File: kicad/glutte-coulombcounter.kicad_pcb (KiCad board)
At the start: 2 copper layers, 100 x 85 mm, 72 parts, among them J1 12V, J2 Measure, J3 K1, J4 AVR-ISP-6, J5 Glutte, J6 K2, J7 K3, J8 Raspi, K1 G6SK-2F-DC5, K2 G6SK-2F-DC5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

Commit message: Minor routing changes
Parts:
- moved C19 2.05 mm to (81.8, 84.1), turned to 270 degrees
- moved C14 0.81 mm to (81.8, 91.4)
- moved C17 0.63 mm to (81.8, 87.6)
- moved C18 0.59 mm to (84.1, 92.5)
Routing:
- net Net-(C19-Pad2): track 5.55 -> 3.92 mm
- net Net-(C18-Pad1): track 7.34 -> 6.15 mm
- net Net-(C14-Pad2): track 4.57 -> 3.97 mm
- net Net-(C14-Pad1): track 4.29 -> 3.69 mm
- net Net-(C17-Pad2): track 4.26 -> 3.75 mm
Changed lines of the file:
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@@
     (thickness 1.6)
     (drawings 152)
-    (tracks 813)
+    (tracks 811)
     (zones 0)
     (modules 72)
@@
   )
   (setup
-    (last_trace_width 0.2)
+    (last_trace_width 0.25)
     (user_trace_width 0.2)
     (user_trace_width 0.25)
@@
     (add_net "Net-(FB1-Pad2)")
     (add_net "Net-(FB2-Pad2)")
-    (add_net "Net-(J5-Pad1)")
     (add_net "Net-(J5-Pad2)")
     (add_net "Net-(J5-Pad3)")
-    (add_net "Net-(J5-Pad4)")
-    (add_net "Net-(J5-Pad6)")
-    (add_net "Net-(J5-Pad7)")
-    (add_net "Net-(J5-Pad8)")
-    (add_net "Net-(J5-Pad9)")
-    (add_net "Net-(J8-Pad1)")
     (add_net "Net-(J8-Pad2)")
     (add_net "Net-(J8-Pad3)")
-    (add_net "Net-(J8-Pad4)")
-    (add_net "Net-(J8-Pad6)")
-    (add_net "Net-(J8-Pad7)")
-    (add_net "Net-(J8-Pad8)")
-    (add_net "Net-(J8-Pad9)")
     (add_net "Net-(K1-Pad12)")
     (add_net "Net-(K1-Pad7)")
@@
     (add_net "Net-(R5-Pad1)")
     (add_net "Net-(R7-Pad1)")
-    (add_net "Net-(U2-Pad1)")
-    (add_net "Net-(U2-Pad3)")
-    (add_net "Net-(U2-Pad5)")
-    (add_net "Net-(U2-Pad7)")
-    (add_net "Net-(U2-Pad8)")
-    (add_net "Net-(U4-Pad4)")
     (add_net "Net-(U6-Pad13)")
     (add_net "Net-(U6-Pad8)")
-    (add_net "Net-(U7-Pad13)")
-    (add_net "Net-(U7-Pad15)")
-    (add_net "Net-(U7-Pad4)")
-    (add_net "Net-(U7-Pad5)")
-    (add_net "Net-(U9-Pad10)")
     (add_net VREF)
   )
@@
   )
   (module Capacitor_SMD:C_0805_2012Metric (layer F.Cu)
-    (at 83.566 83.058 180)
+    (at 81.788 84.074 270)
     (descr "Capacitor SMD 0805 (2012 Metric), square (rectangular) end terminal, IPC_7351 nominal, (Body size source: https://docs.google.com/spreadsheets/d/1BsfQQcO9C6DZCsRaXUlFlo91Tg2WpOkGARC1WS5S8t0/edit?usp=sharing), generated with kicad-footprint-generator")
     (tags capacitor)
     (attr smd)
-    (fp_text reference C19 (at 0 -1.65) (layer F.SilkS)
+    (fp_text reference C19 (at 0 -1.65 90) (layer F.SilkS)
       (effects (font (size 1 1) (thickness 0.15)))
     )
-    (fp_text value 1u (at 0 1.65) (layer F.Fab)
+    (fp_text value 1u (at 0 1.65 90) (layer F.Fab)
       (effects (font (size 1 1) (thickness 0.15)))
     )
-    (fp_text user %R (at 0 0) (layer F.Fab)
+    (fp_text user %R (at 0 0 90) (layer F.Fab)
       (effects (font (size 0.5 0.5) (thickness 0.08)))
     )
@@
     (fp_line (start -1 -0.6) (end 1 -0.6) (layer F.Fab) (width 0.1))
     (fp_line (start -1 0.6) (end -1 -0.6) (layer F.Fab) (width 0.1))
-    (pad 2 smd roundrect (at 0.9375 0 180) (size 0.975 1.4) (layers F.Cu F.Paste F.Mask) (roundrect_rratio 0.25)
+    (pad 2 smd roundrect (at 0.9375 0 270) (size 0.975 1.4) (layers F.Cu F.Paste F.Mask) (roundrect_rratio 0.25)
       (net 18 "Net-(C19-Pad2)"))
-    (pad 1 smd roundrect (at -0.9375 0 180) (size 0.975 1.4) (layers F.Cu F.Paste F.Mask) (roundrect_rratio 0.25)
+    (pad 1 smd roundrect (at -0.9375 0 270) (size 0.975 1.4) (layers F.Cu F.Paste F.Mask) (roundrect_rratio 0.25)
       (net 1 GNDA))
     (model ${KISYS3DMOD}/Capacitor_SMD.3dshapes/C_0805_2012Metric.wrl
@@
   )
   (module Capacitor_SMD:C_0805_2012Metric (layer F.Cu)
-    (at 84.608 92.202 270)
+    (at 84.074 92.456 270)
     (descr "Capacitor SMD 0805 (2012 Metric), square (rectangular) end terminal, IPC_7351 nominal, (Body size source: https://docs.google.com/spreadsheets/d/1BsfQQcO9C6DZCsRaXUlFlo91Tg2WpOkGARC1WS5S8t0/edit?usp=sharing), generated with kicad-footprint-generator")
     (tags capacitor)
@@
   )
   (module Capacitor_SMD:C_0805_2012Metric (layer F.Cu)
-    (at 82.068 87.065 90)
+    (at 81.788 87.63 90)
     (descr "Capacitor SMD 0805 (2012 Metric), square (rectangular) end terminal, IPC_7351 nominal, (Body size source: https://docs.google.com/spreadsheets/d/1BsfQQcO9C6DZCsRaXUlFlo91Tg2WpOkGARC1WS5S8t0/edit?usp=sharing), generated with kicad-footprint-generator")
     (tags capacitor)
     (attr smd)
-    (fp_text reference C17 (at 0 -1.65 90) (layer F.SilkS)
+    (fp_text reference C17 (at 0 1.778 90) (layer F.SilkS)
       (effects (font (size 1 1) (thickness 0.15)))
     )
@@
   )
   (module Capacitor_SMD:C_0805_2012Metric (layer F.Cu)
-    (at 82.068 92.202 90)
+    (at 81.788 91.44 90)
     (descr "Capacitor SMD 0805 (2012 Metric), square (rectangular) end terminal, IPC_7351 nominal, (Body size source: https://docs.google.com/spreadsheets/d/1BsfQQcO9C6DZCsRaXUlFlo91Tg2WpOkGARC1WS5S8t0/edit?usp=sharing), generated with kicad-footprint-generator")
     (tags capacitor)
     (attr smd)
-    (fp_text reference C14 (at 0 -1.65 90) (layer F.SilkS)
+    (fp_text reference C14 (at -2.54 -0.254 180) (layer F.SilkS)
       (effects (font (size 1 1) (thickness 0.15)))
     )
@@
   (via (at 80.264 95.504) (size 0.8) (drill 0.4) (layers F.Cu B.Cu) (net 1))
   (via (at 71.882 93.98) (size 0.8) (drill 0.4) (layers F.Cu B.Cu) (net 1))
-  (via (at 86.106 92.71) (size 0.8) (drill 0.4) (layers F.Cu B.Cu) (net 1))
-  (via (at 87.884 83.058) (size 0.8) (drill 0.4) (layers F.Cu B.Cu) (net 1))
+  (via (at 84.074 94.742) (size 0.8) (drill 0.4) (layers F.Cu B.Cu) (net 1))
+  (via (at 81.788 81.534) (size 0.8) (drill 0.4) (layers F.Cu B.Cu) (net 1))
   (via (at 85.09 66.04) (size 0.8) (drill 0.4) (layers F.Cu B.Cu) (net 1))
   (via (at 97.5 95) (size 0.8) (drill 0.4) (layers F.Cu B.Cu) (net 1))
@@
   (segment (start 56.8175 61.468) (end 60.2345 61.468) (width 0.4) (layer F.Cu) (net 11))
   (segment (start 60.2345 61.468) (end 60.325 61.3775) (width 0.4) (layer F.Cu) (net 11))
-  (segment (start 80.3805 89.605) (end 82.068 91.2925) (width 0.25) (layer F.Cu) (net 12))
-  (segment (start 78.193 89.605) (end 80.3805 89.605) (width 0.25) (layer F.Cu) (net 12))
-  (segment (start 78.193 92.145) (end 79.9455 92.145) (width 0.25) (layer F.Cu) (net 13))
-  (segment (start 80.94 93.1395) (end 82.068 93.1395) (width 0.25) (layer F.Cu) (net 13))
-  (segment (start 79.9455 92.145) (end 80.94 93.1395) (width 0.25) (layer F.Cu) (net 13))
+  (segment (start 80.5965 90.5025) (end 81.788 90.5025) (width 0.25) (layer F.Cu) (net 12))
+  (segment (start 78.193 89.605) (end 79.699 89.605) (width 0.25) (layer F.Cu) (net 12))
+  (segment (start 79.699 89.605) (end 80.5965 90.5025) (width 0.25) (layer F.Cu) (net 12))
+  (segment (start 81.5555 92.145) (end 81.788 92.3775) (width 0.25) (layer F.Cu) (net 13))
+  (segment (start 78.193 92.145) (end 81.5555 92.145) (width 0.25) (layer F.Cu) (net 13))
   (via (at 44.196 59.436) (size 0.8) (drill 0.4) (layers F.Cu B.Cu) (net 14))
   (segment (start 44.45 59.69) (end 44.45 61.7) (width 0.25) (layer F.Cu) (net 14))
@@
   (segment (start 74.7545 43.18) (end 78.105 43.18) (width 0.4) (layer F.Cu) (net 14))
   (segment (start 74.676 43.2585) (end 74.7545 43.18) (width 0.4) (layer F.Cu) (net 14))
-  (segment (start 81.518 86.1275) (end 82.068 86.1275) (width 0.25) (layer F.Cu) (net 15))
-  (segment (start 78.193 87.065) (end 80.5805 87.065) (width 0.25) (layer F.Cu) (net 15))
-  (segment (start 80.5805 87.065) (end 81.518 86.1275) (width 0.25) (layer F.Cu) (net 15))
-  (segment (start 81.7355 88.335) (end 82.068 88.0025) (width 0.25) (layer F.Cu) (net 16))
-  (segment (start 78.193 88.335) (end 81.7355 88.335) (width 0.25) (layer F.Cu) (net 16))
-  (segment (start 83.836653 92.063847) (end 84.608 91.2925) (width 0.25) (layer F.Cu) (net 17))
-  (segment (start 81.07681 92.202) (end 83.6985 92.202) (width 0.25) (layer F.Cu) (net 17))
-  (segment (start 78.193 90.875) (end 79.74981 90.875) (width 0.25) (layer F.Cu) (net 17))
-  (segment (start 83.6985 92.202) (end 83.836653 92.063847) (width 0.25) (layer F.Cu) (net 17))
-  (segment (start 79.74981 90.875) (end 81.07681 92.202) (width 0.25) (layer F.Cu) (net 17))
-  (segment (start 79.870002 85.795) (end 82.607002 83.058) (width 0.25) (layer F.Cu) (net 18))
-  (segment (start 78.193 85.795) (end 79.870002 85.795) (width 0.25) (layer F.Cu) (net 18))
+  (segment (start 78.193 87.065) (end 80.067 87.065) (width 0.25) (layer F.Cu) (net 15))
+  (segment (start 80.4395 86.6925) (end 81.788 86.6925) (width 0.25) (layer F.Cu) (net 15))
+  (segment (start 80.067 87.065) (end 80.4395 86.6925) (width 0.25) (layer F.Cu) (net 15))
+  (segment (start 80.1855 88.5675) (end 81.788 88.5675) (width 0.25) (layer F.Cu) (net 16))
+  (segment (start 78.193 88.335) (end 79.953 88.335) (width 0.25) (layer F.Cu) (net 16))
+  (segment (start 79.953 88.335) (end 80.1855 88.5675) (width 0.25) (layer F.Cu) (net 16))
+  (segment (start 78.8365 91.5185) (end 84.074 91.5185) (width 0.25) (layer F.Cu) (net 17))
+  (segment (start 78.193 90.875) (end 78.8365 91.5185) (width 0.25) (layer F.Cu) (net 17))
+  (segment (start 81.0045 85.795) (end 81.788 85.0115) (width 0.25) (layer F.Cu) (net 18))
+  (segment (start 78.193 85.795) (end 81.0045 85.795) (width 0.25) (layer F.Cu) (net 18))
   (segment (start 63.246 29.126) (end 63.246 25.599) (width 0.4) (layer F.Cu) (net 19))
   (segment (start 61.957 29.49) (end 62.882 29.49) (width 0.4) (layer F.Cu) (net 19))

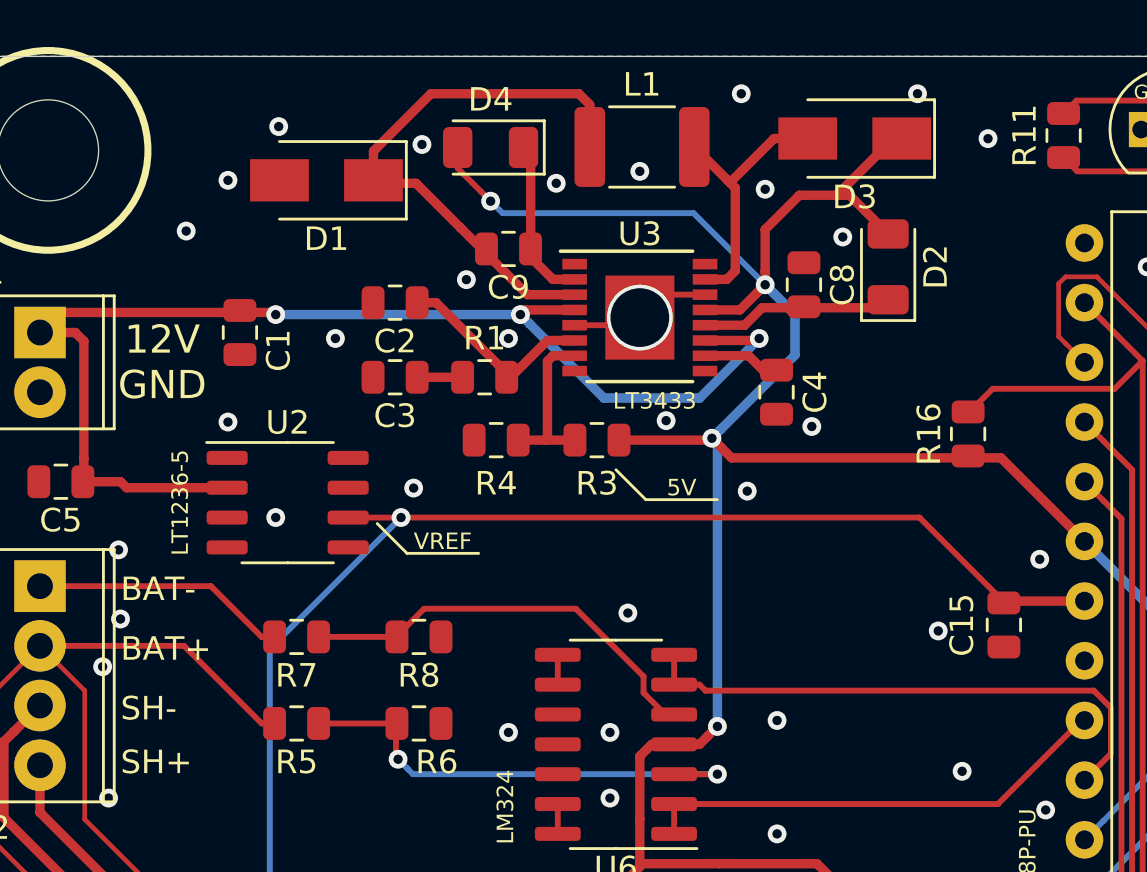
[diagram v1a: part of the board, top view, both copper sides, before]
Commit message: Correct wrong DCDC inductor
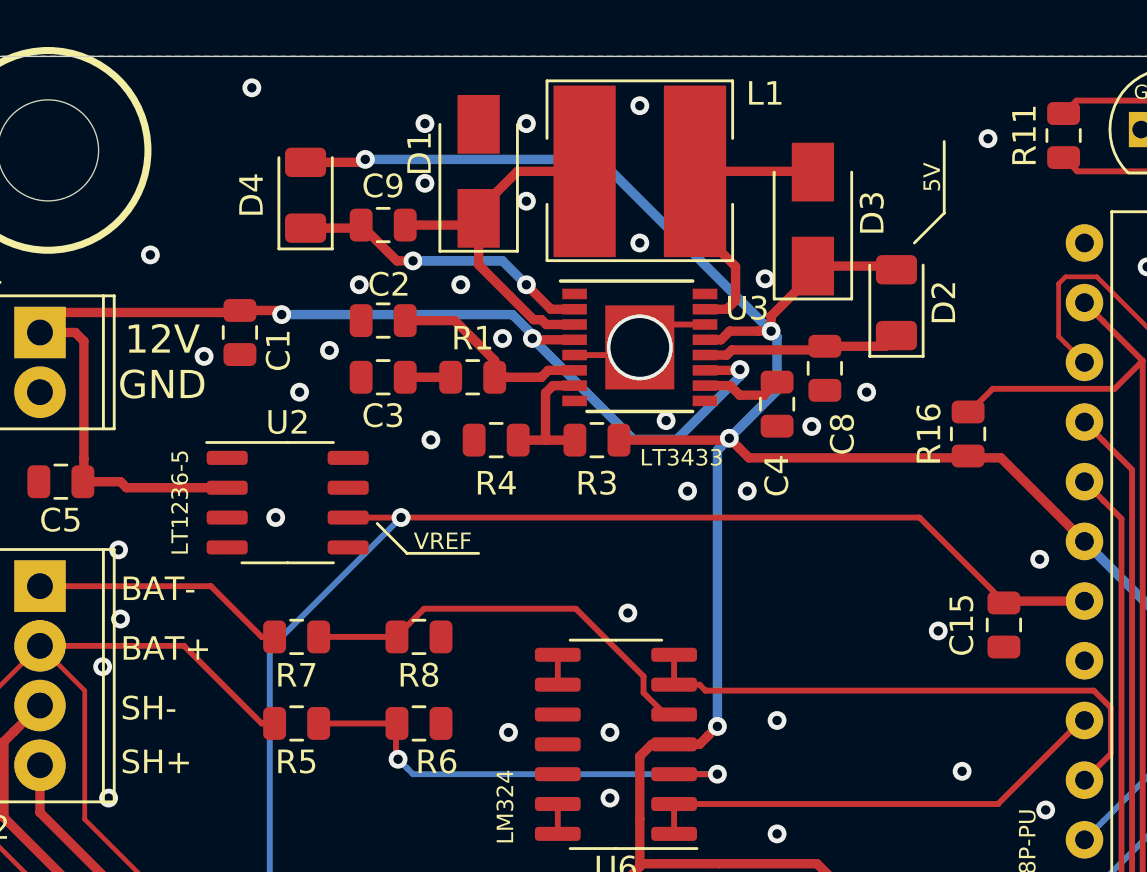
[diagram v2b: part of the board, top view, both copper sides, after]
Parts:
- L1: footprint Inductor_SMD:L_1812_4532Metric_Pad1.30x3.40mm_HandSolder -> glutte-coulombcounter:Sumida_CDRH6D28
- moved D4 8.13 mm to (45.0, 25.9), turned to 90 degrees
- moved D1 6.49 mm to (52.3, 24.9), turned to 90 degrees
- moved C9 5.43 mm to (48.3, 27.2), turned to 0 degrees
- moved D3 3.86 mm to (66.5, 26.9), turned to 90 degrees
- moved C8 3.67 mm to (67.1, 33.3), turned to 90 degrees
- moved D2 1.56 mm to (70.1, 30.5)
- moved U3 1.27 mm to (59.2, 32.4)
- moved L1 1.04 mm to (59.2, 24.9)
- moved C2 0.92 mm to (48.3, 31.2)
- moved C4 0.51 mm to (65.0, 34.8)
- moved C3 0.51 mm to (48.3, 33.7)
- moved R1 0.51 mm to (52.1, 33.7)
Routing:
- net Net-(C9-Pad2): track 24.0 -> 15.9 mm
- net Net-(C9-Pad1): track 7.06 -> 13.0 mm, vias 0 -> 2
- net +5VA: track 348.2 -> 346.6 mm
- net +12V: track 52.5 -> 51.2 mm
- net Net-(R3-Pad1): track 7.06 -> 5.78 mm
- net Net-(D3-Pad2): track 11.5 -> 12.7 mm
- net Net-(C2-Pad1): track 8.66 -> 9.22 mm
- net GNDA: vias 138 -> 141

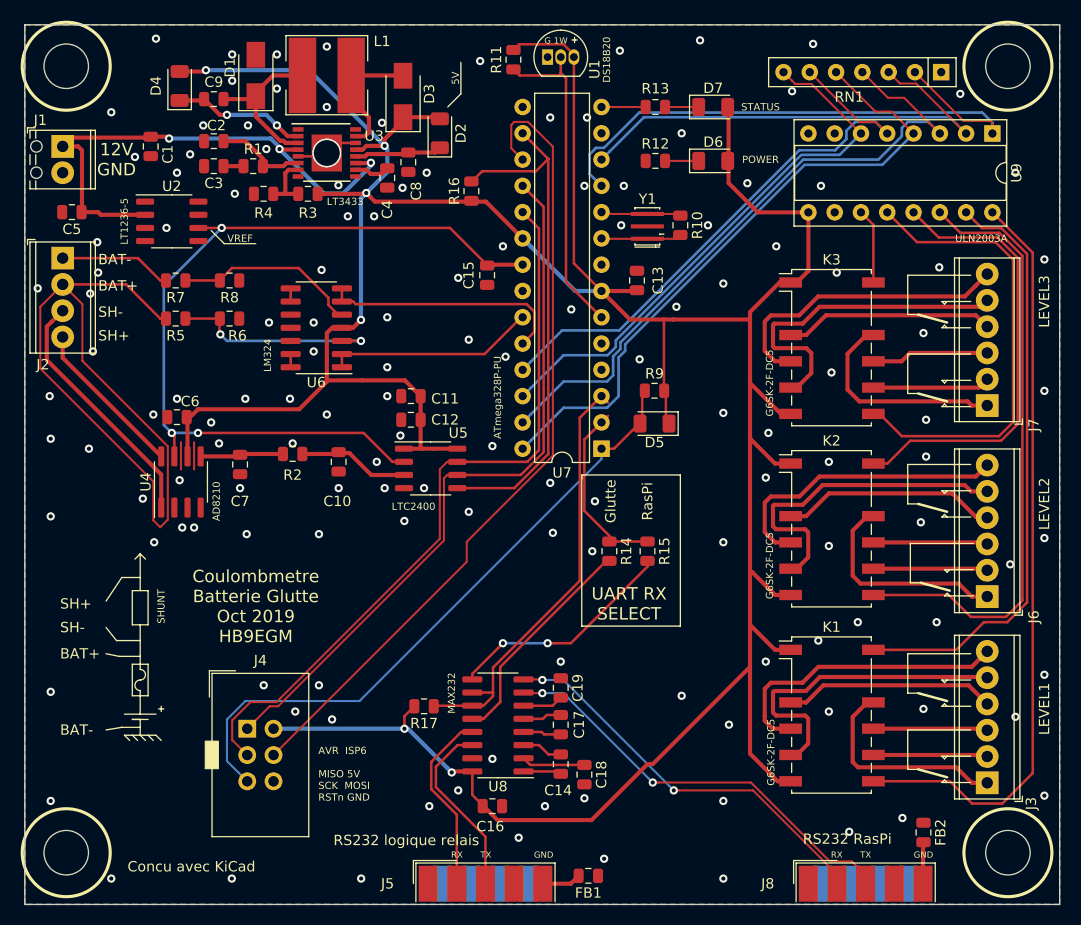
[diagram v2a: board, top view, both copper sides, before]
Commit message: Add Ampere to back silkscreen and update MPN
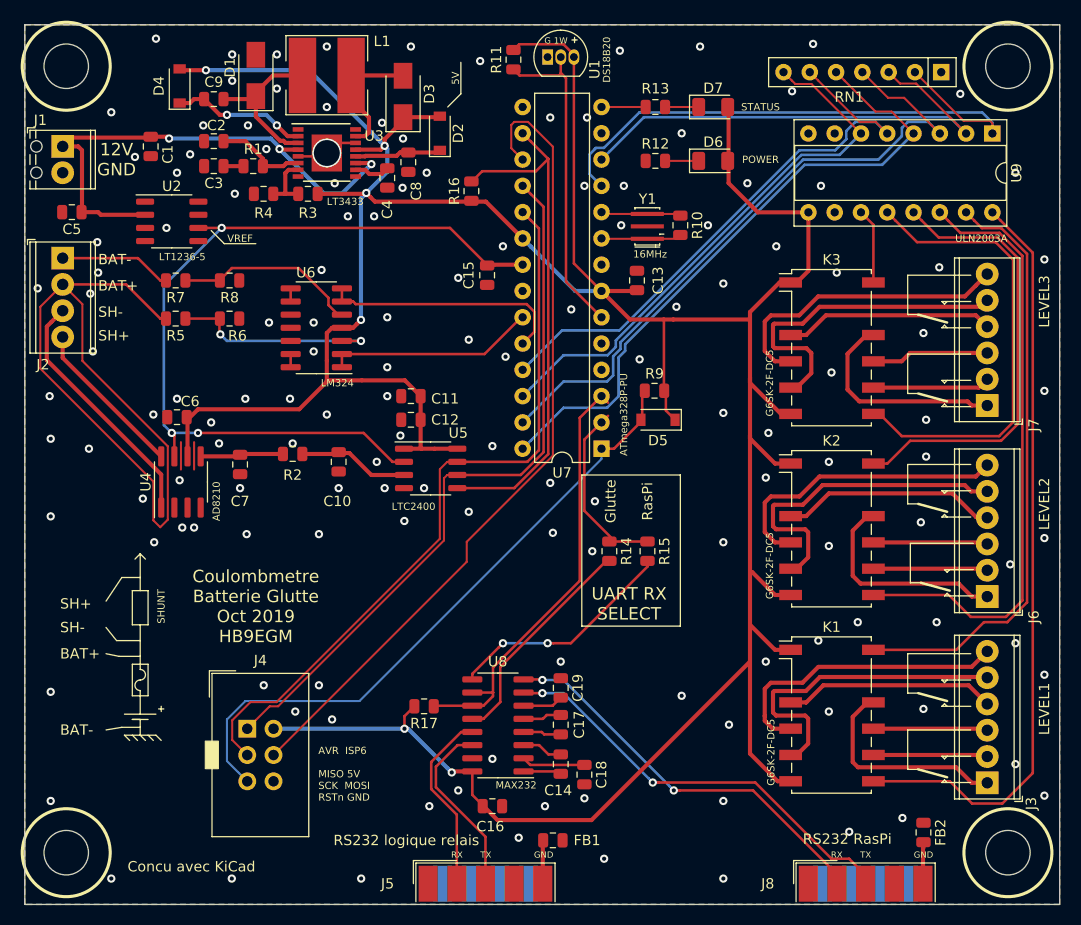
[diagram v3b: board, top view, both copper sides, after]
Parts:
- added G***: LOGO, glutte-coulombcounter:ampere, B.Cu at (55.1, 55.4)
- D2, D4, D5: footprint Diode_SMD:D_1206_3216Metric -> Diode_SMD:D_SOD-123
- RN1: value 470R -> 2k2
- moved FB1 4.85 mm to (81.0, 98.8)
- moved D5 0.50 mm to (91.2, 58.2)
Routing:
- net GNDA: vias 141 -> 144
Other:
- board text added: "16MHz"
- board text added: "André-Marie Ampère 1775 - 1836"
